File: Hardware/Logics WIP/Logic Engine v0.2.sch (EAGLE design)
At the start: 36 parts, among them IC1 MEGA328P, Y1 16MHz

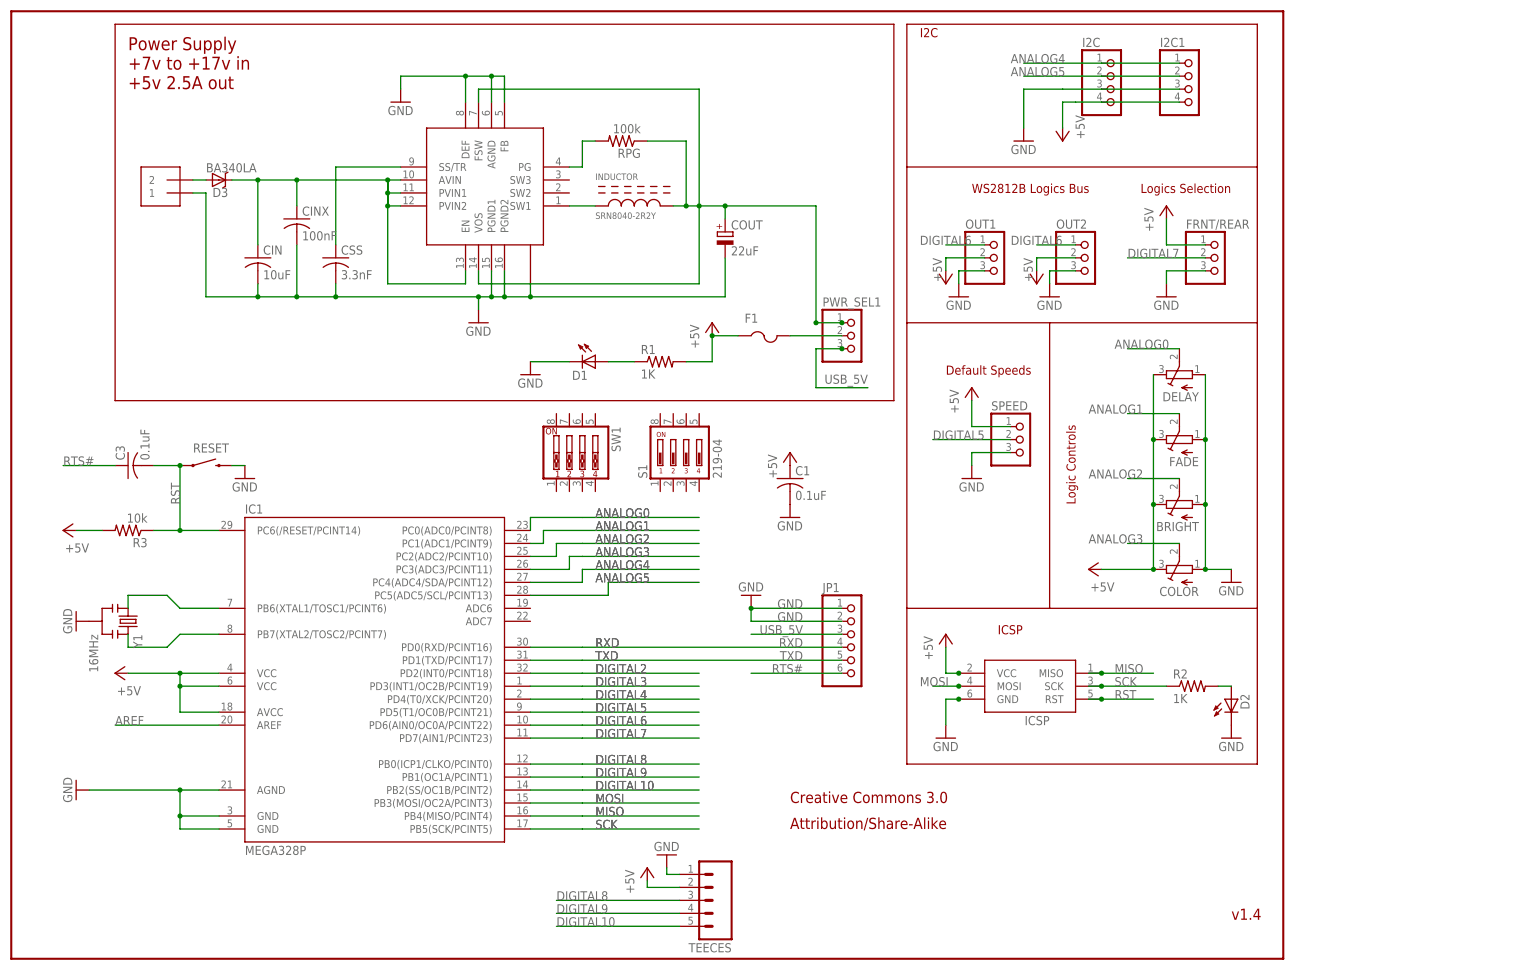
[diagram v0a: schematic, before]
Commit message: added microSD card holder to the RSeries library and Logic Engine (still unfinished)
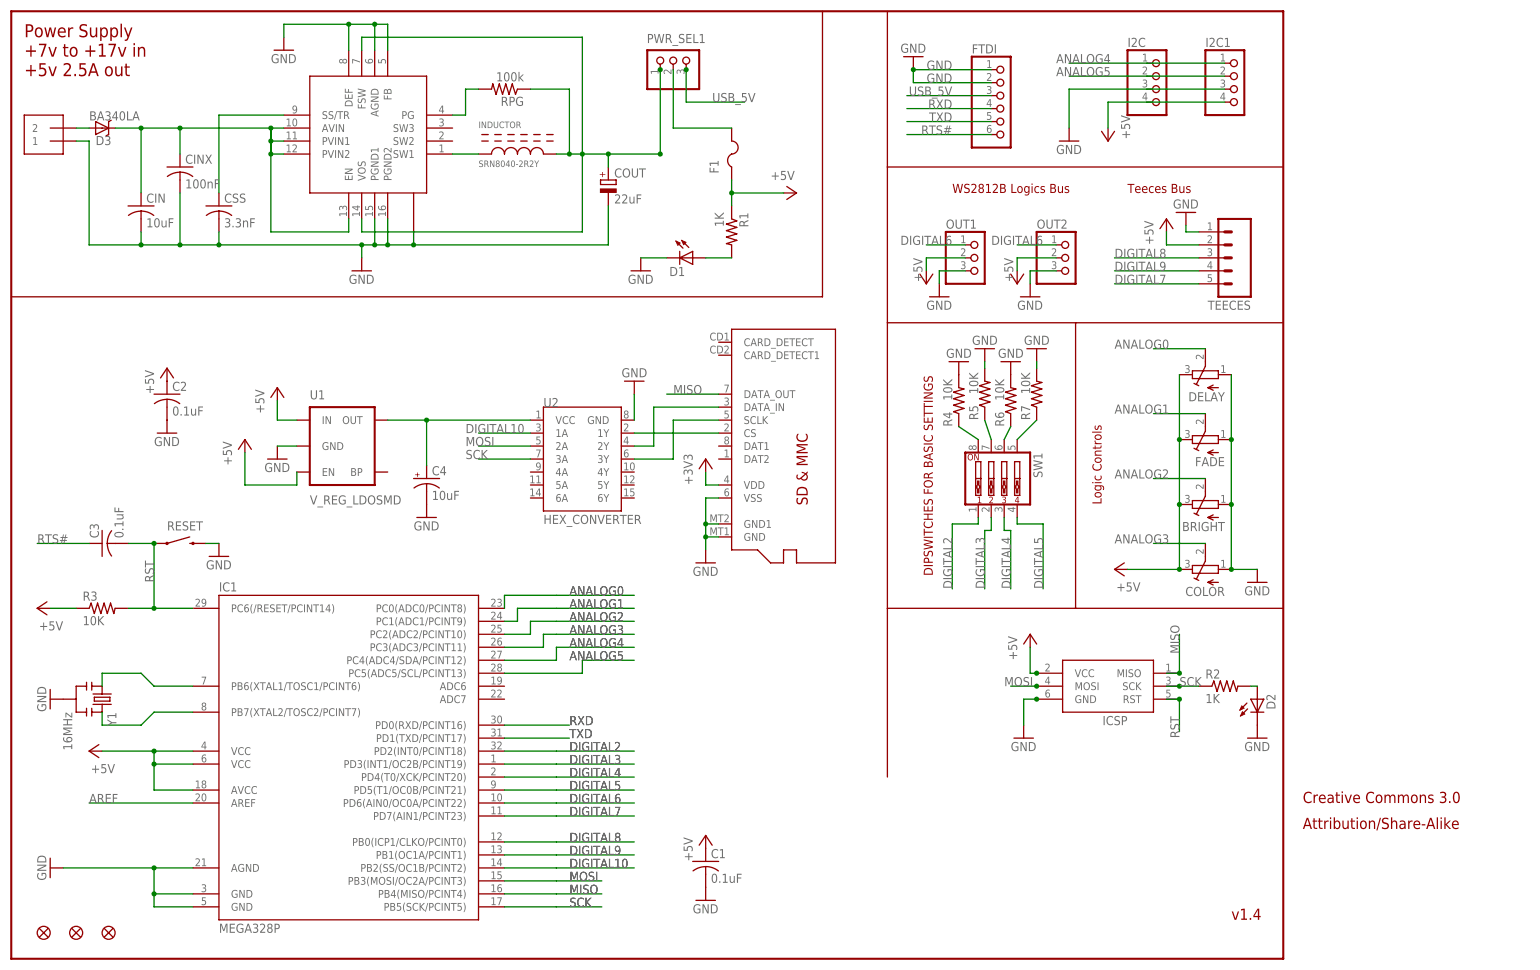
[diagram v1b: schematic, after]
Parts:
- removed FRNT/REAR, SPEED: (no value), pinhead:PINHD-1X3
- removed JP1: (no value), carduino:PINHD-1X6CLEAN
- removed S1: 219-04, switch-dil:219-04
- added C2: 0.1uF, adafruit:C-USC0805K
- added C4: 10uF, SparkFun-Capacitors:10UF-16V-10%(TANT)
- added FID1, FID2, FID3: FIDUCIAL1X2.5, SparkFun-Aesthetics:FIDUCIAL1X2.5
- added FTDI: (no value), carduino:PINHD-1X6CLEAN
- added R4, R5, R6, R7: 10K, SparkFun-Resistors:RESISTOR0603
- added U$1: MICROSD, rseries:MICROSD
- added U1: V_REG_LDOSMD, SparkFun-PowerIC:V_REG_LDOSMD
- added U2: HEX_CONVERTER, SparkFun-DigitalIC:HEX_CONVERTER
- R1, R2: device adafruit:R-US_R0805 -> SparkFun-Resistors:RESISTOR0603
- R3: value 10k -> 10K; device adafruit:R-US_R0805 -> SparkFun-Resistors:RESISTOR0603
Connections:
- new net N$12: R4.1, SW1.8
- new net N$13: R5.1, SW1.7
- new net N$14: R6.1, SW1.6
- new net N$15: R7.1, SW1.5
- new net N$16: U$1.DATA_IN, U2.2Y
- new net N$17: U$1.SCLK, U2.3Y
- new net N$18: U$1.CS, U2.1Y
- new net N$19: C4.+, U1.OUT, U2.VCC
- net +5V: now also C2.1, R1.1, R3.1, U$1.VDD, U1.EN, U1.IN; no longer FRNT/REAR.1, R1.2, R3.2, SPEED.1
- net DIGITAL10: now also U2.1A; no longer TEECES.5
- net DIGITAL2: now also SW1.1
- net DIGITAL3: now also SW1.2
- net DIGITAL4: now also SW1.3
- net DIGITAL5: now also SW1.4; no longer SPEED.2
- net DIGITAL7: now also TEECES.5; no longer FRNT/REAR.2
- net GND: now also C2.2, C4.-, FTDI.1, FTDI.2, R4.2, R5.2, R6.2, R7.2, U$1.GND, U$1.GND1, U$1.VSS, U1.GND, U2.GND; no longer FRNT/REAR.3, JP1.1, JP1.2, SPEED.3
- net MISO: now also U$1.DATA_OUT
- net MOSI: now also U2.2A
- net N$5: now also R1.2; no longer R1.1
- net RST: now also R3.2; no longer R3.1
- net RTS#: now also FTDI.6; no longer JP1.6
- net RXD: now also FTDI.4; no longer JP1.4
- net SCK: now also U2.3A
- net TXD: now also FTDI.5; no longer JP1.5
- net USB_5V: now also FTDI.3; no longer JP1.3
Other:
- note added: "DIPSWITCHES FOR BASIC SETTINGS"
- note added: "Teeces Bus"
- note removed: "Default Speeds"
- note removed: "I2C"
- note removed: "ICSP"
- note removed: "Logics Selection"
- moved on the sheet: BRIGHT, C1, C3, CIN, CINX, COLOR, COUT, CSS, D1, D2, D3, DELAY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
